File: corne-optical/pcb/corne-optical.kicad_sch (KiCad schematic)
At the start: 62 parts, among them J1 Conn_01x04, J2 Conn_01x03, J3 MJ-4PP-9, J4 Conn_01x01, J5 Conn_01x01, J6 Conn_01x02, J7 Conn_01x02, Q1 Q_NMOS_GSD, Q2 Q_NMOS_GSD, Q3 Q_NMOS_GSD, Q4 Q_NMOS_GSD, Q5 Q_NMOS_GSD, Q6 Q_NMOS_GSD, SW1 Keychron_LP_Optical, SW10 Keychron_LP_Optical, SW11 Keychron_LP_Optical, SW12 Keychron_LP_Optical, SW13 Keychron_LP_Optical, SW14 Keychron_LP_Optical, SW15 Keychron_LP_Optical, SW16 Keychron_LP_Optical, SW17 Keychron_LP_Optical, SW18 Keychron_LP_Optical, SW19 Keychron_LP_Optical, SW2 Keychron_LP_Optical, SW20 Keychron_LP_Optical, SW21 Keychron_LP_Optical, SW3 Keychron_LP_Optical, SW4 Keychron_LP_Optical, SW5 Keychron_LP_Optical, SW6 Keychron_LP_Optical, SW7 Keychron_LP_Optical, SW8 Keychron_LP_Optical, SW9 Keychron_LP_Optical, U1 ProMicro

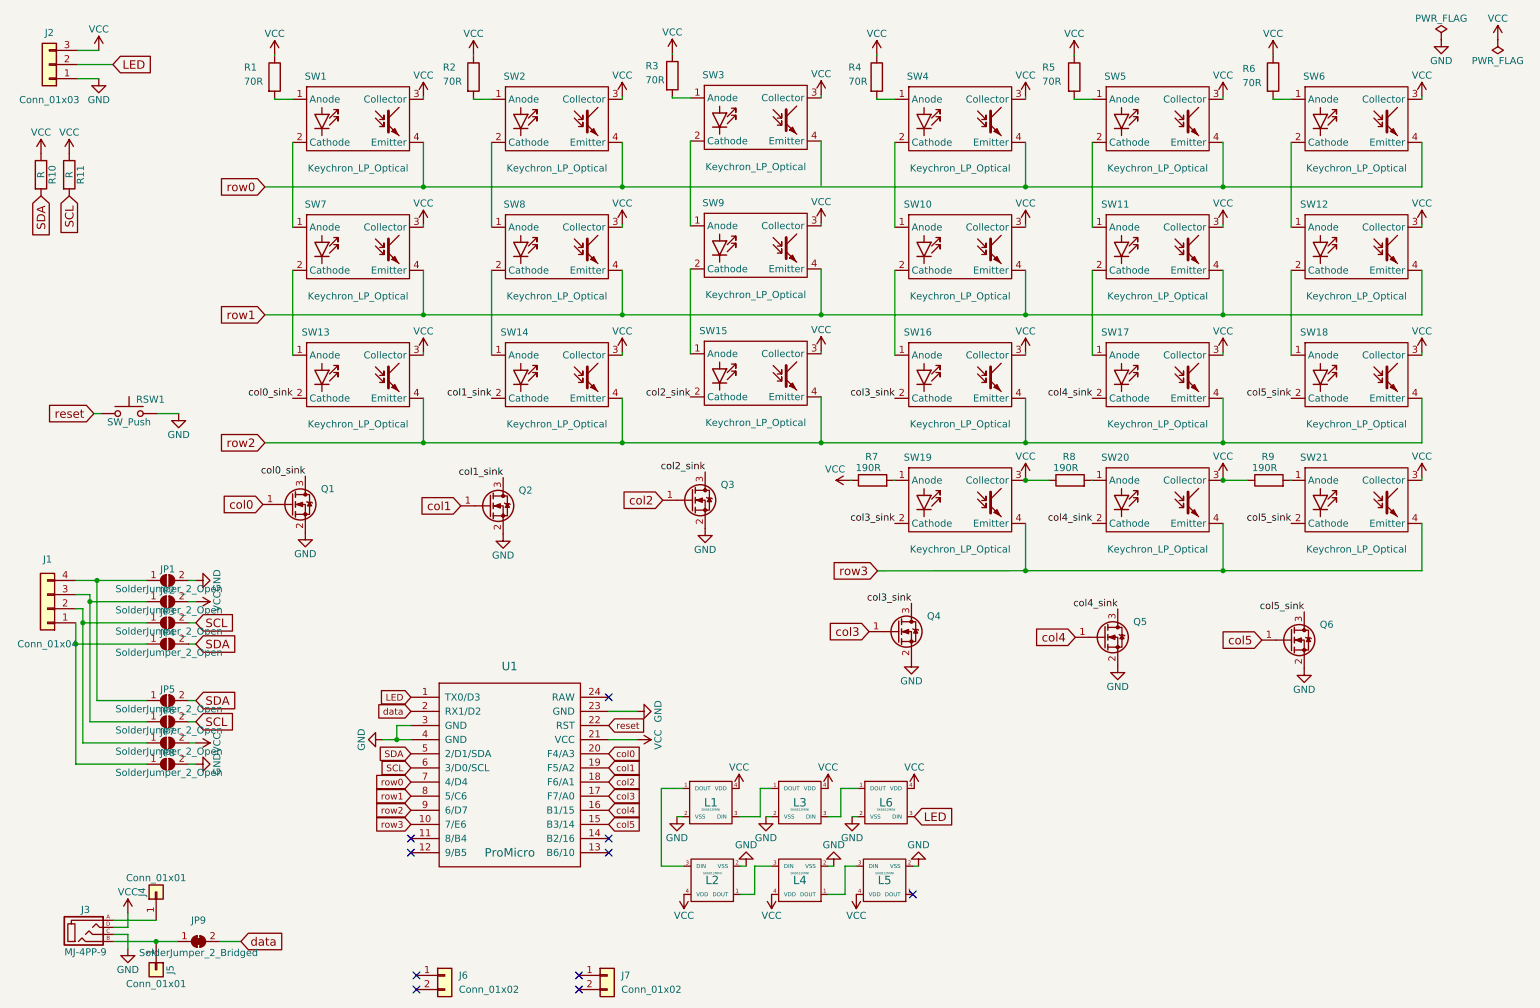
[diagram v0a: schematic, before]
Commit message: Fixed up designators on optical
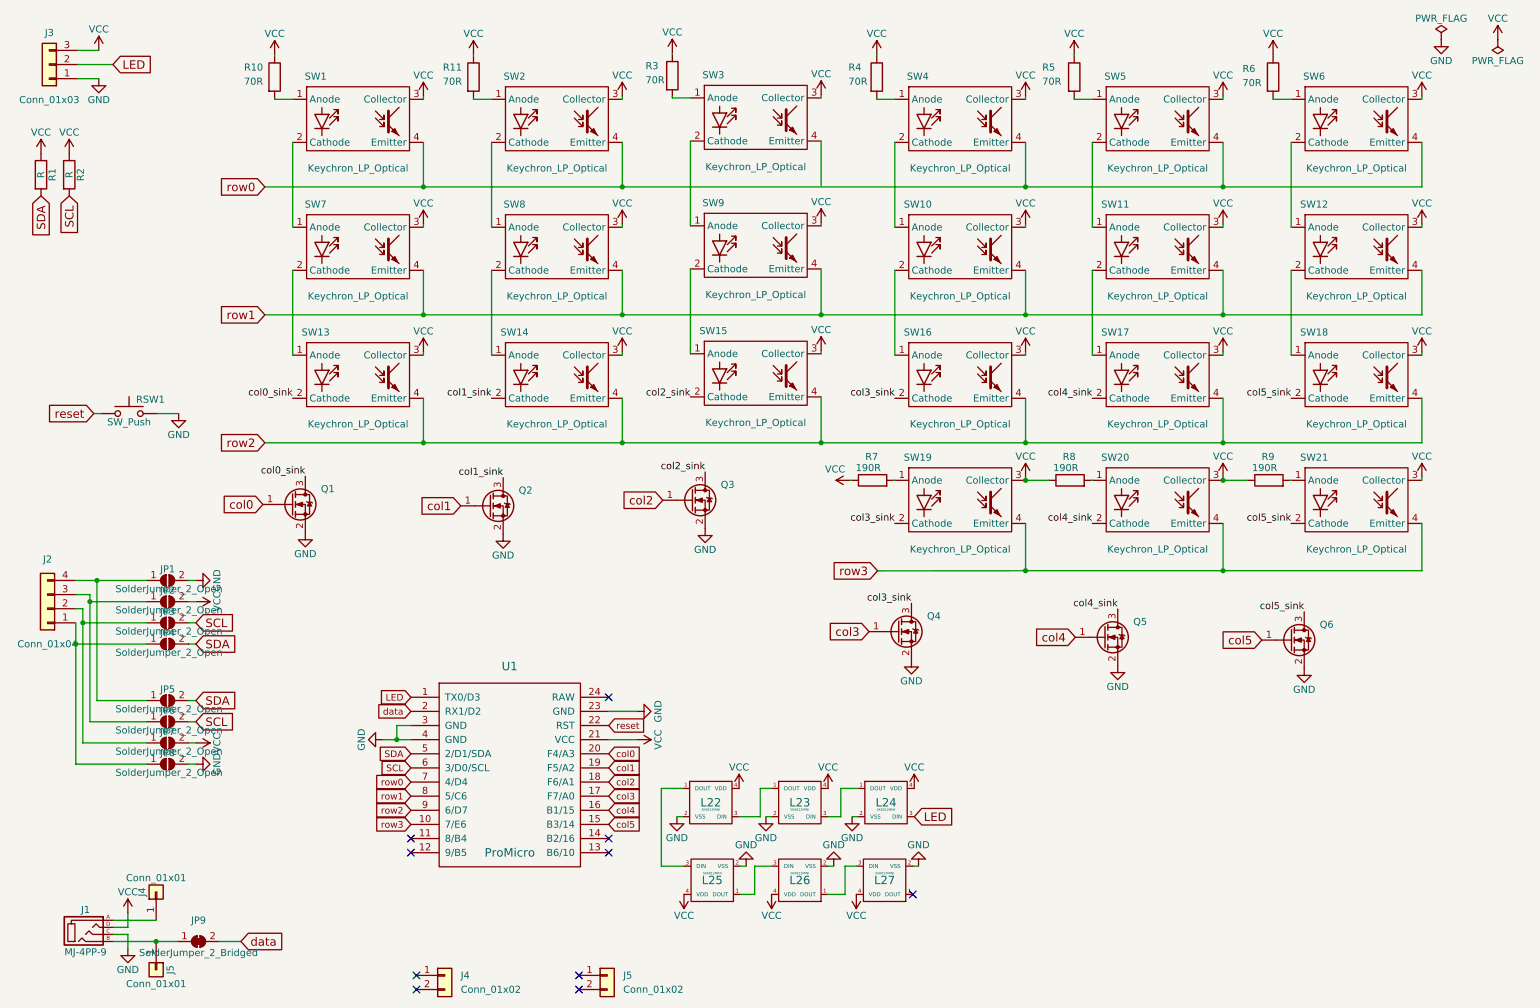
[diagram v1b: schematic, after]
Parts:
- renumbered J3 to J1, J1 to J2, J2 to J3, J6 to J4, J7 to J5, L1 to L22, L3 to L23, L6 to L24, L2 to L25, L4 to L26, L5 to L27, R10 to R1, R1 to R10, R2 to R11, R11 to R2

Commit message: Missed a few
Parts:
- renumbered JP9 to JP1, JP1 to JP9, J4 to P1, J5 to P2
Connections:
- net GND: now also JP2.2 (B); no longer JP8.2 (B)
- net SCL: now also JP4.2 (B), JP7.2 (B); no longer JP3.2 (B), JP6.2 (B)
- net SDA: now also JP6.2 (B); no longer JP4.2 (B)
- net VCC: now also JP3.2 (B), JP8.2 (B); no longer JP2.2 (B), JP7.2 (B)
- net at JP4.1 (A), JP8.1 (A): now also J2.2 (Pin_2); no longer J2.1 (Pin_1)
- net at JP3.1 (A), JP7.1 (A): now also J2.3 (Pin_3); no longer J2.2 (Pin_2)
- net at JP2.1 (A), JP6.1 (A): now also J2.4 (Pin_4); no longer J2.3 (Pin_3)
- net at JP5.1 (A), JP9.1 (A): now also J2.1 (Pin_1); no longer J2.4 (Pin_4)
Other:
- moved on the sheet: JP2, JP3, JP4, JP5, JP6, JP7, JP8, JP9

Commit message: Trying to workout phantom copper
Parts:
- removed L22, L23, L24, L25, L26, L27: SK6812MINI, kbd:SK6812MINI_underglow_rev, symbol kbd:SK6812MINI
- SW1, SW10, SW11, SW12, SW13, SW14, SW15, SW16, SW17, SW18, SW19, SW2, SW20, SW3, SW4, SW5, SW6, SW7, SW8, SW9: footprint kbd:Choc_Hotswap -> optical:Keychron_LP_Optical
- SW21: footprint kbd:Choc_Hotswap_1.5u -> optical:Keychron_LP_Optical_1.5u
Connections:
- no-connect marks 10 -> 9

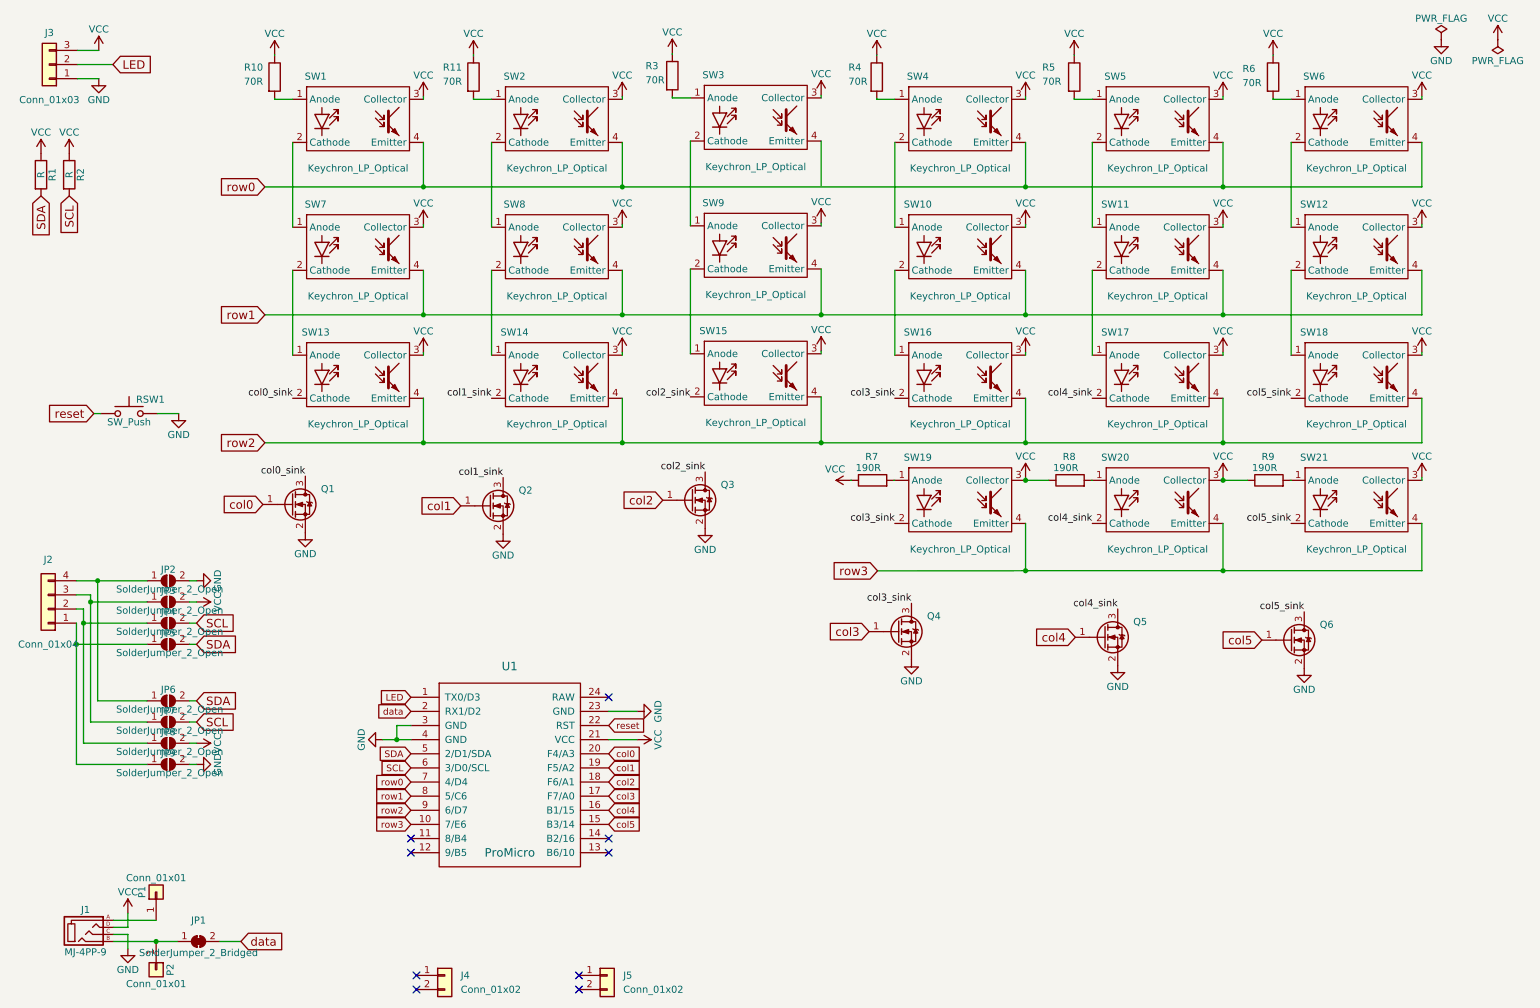
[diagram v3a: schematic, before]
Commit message: Fixed outline, just trying to solve switch footprint glitch
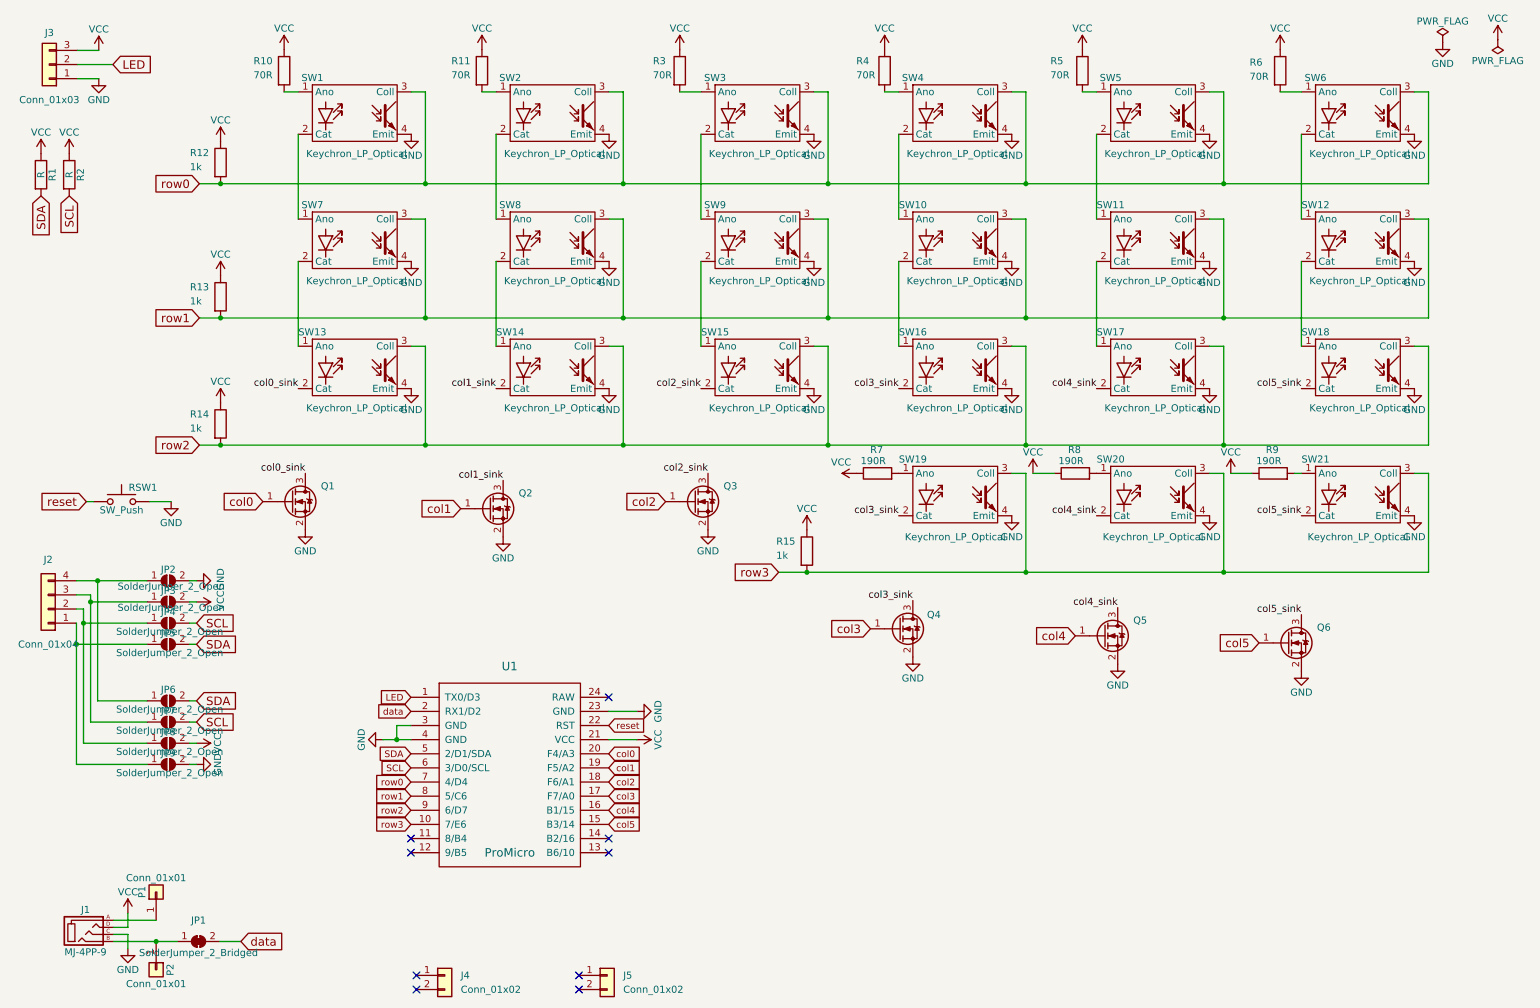
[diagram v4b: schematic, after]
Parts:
- added R12, R13, R14, R15: 1k, Resistor_SMD:R_0603_1608Metric, symbol Device:R
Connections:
- net GND: now also SW1.4 (Emit), SW10.4 (Emit), SW11.4 (Emit), SW12.4 (Emit), SW13.4 (Emit), SW14.4 (Emit), SW15.4 (Emit), SW16.4 (Emit), SW17.4 (Emit), SW18.4 (Emit), SW19.4 (Emit), SW2.4 (Emit), SW20.4 (Emit), SW21.4 (Emit), SW3.4 (Emit), SW4.4 (Emit), SW5.4 (Emit), SW6.4 (Emit), SW7.4 (Emit), SW8.4 (Emit), SW9.4 (Emit)
- net VCC: now also R12.1, R13.1, R14.1, R15.1; no longer SW1.3 (Collector), SW10.3 (Collector), SW11.3 (Collector), SW12.3 (Collector), SW13.3 (Collector), SW14.3 (Collector), SW15.3 (Collector), SW16.3 (Collector), SW17.3 (Collector), SW18.3 (Collector), SW19.3 (Collector), SW2.3 (Collector), SW20.3 (Collector), SW21.3 (Collector), SW3.3 (Collector), SW4.3 (Collector), SW5.3 (Collector), SW6.3 (Collector), SW7.3 (Collector), SW8.3 (Collector), SW9.3 (Collector)
- net col2_sink: now also SW15.2 (Cat)
- net row0: now also SW1.3 (Coll), SW2.3 (Coll), SW3.3 (Coll), SW4.3 (Coll), SW5.3 (Coll), SW6.3 (Coll), R12.2; no longer SW1.4 (Emitter), SW2.4 (Emitter), SW4.4 (Emitter), SW5.4 (Emitter), SW6.4 (Emitter)
- net row1: now also SW10.3 (Coll), SW11.3 (Coll), SW12.3 (Coll), SW7.3 (Coll), SW8.3 (Coll), SW9.3 (Coll), R13.2; no longer SW10.4 (Emitter), SW11.4 (Emitter), SW12.4 (Emitter), SW7.4 (Emitter), SW8.4 (Emitter), SW9.4 (Emitter)
- net row2: now also SW13.3 (Coll), SW14.3 (Coll), SW15.3 (Coll), SW16.3 (Coll), SW17.3 (Coll), SW18.3 (Coll), R14.2; no longer SW13.4 (Emitter), SW14.4 (Emitter), SW15.4 (Emitter), SW16.4 (Emitter), SW17.4 (Emitter), SW18.4 (Emitter)
- net row3: now also SW19.3 (Coll), SW20.3 (Coll), SW21.3 (Coll), R15.2; no longer SW19.4 (Emitter), SW20.4 (Emitter), SW21.4 (Emitter)
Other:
- moved on the sheet: Q1, Q2, Q3, Q4, Q6, R10, R11, R3, R4, R5, R6, R7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

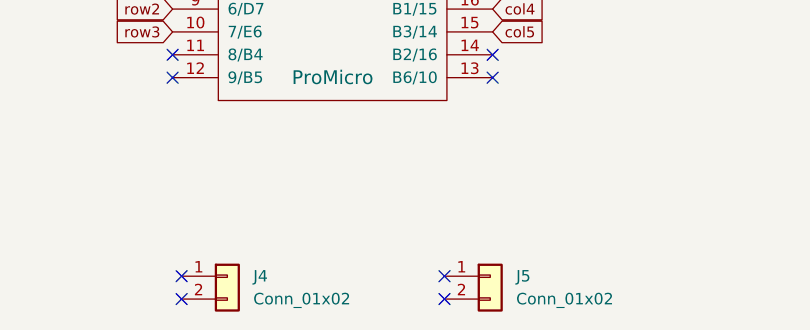
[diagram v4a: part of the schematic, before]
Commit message: Finished, but need to add mounting holes for plate
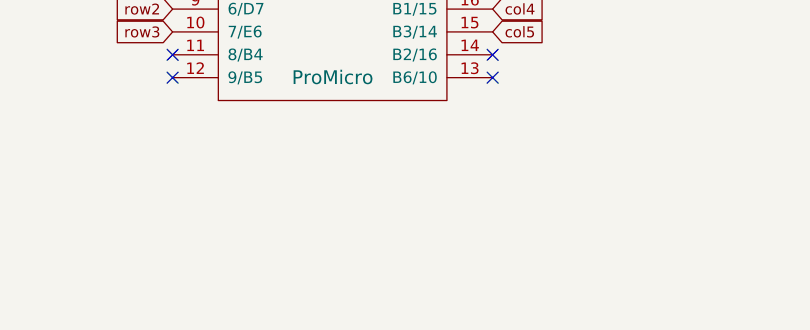
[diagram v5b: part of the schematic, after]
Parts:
- removed J4, J5: Conn_01x02, Connector_AMASS:AMASS_XT60-F_1x02_P7.20mm_Vertical, symbol Connector_Generic:Conn_01x02
- Q1, Q2, Q3, Q4, Q5, Q6: footprint Package_TO_SOT_SMD:SOT-23 -> optical:SOT-23
- R1, R2: footprint kbd:R -> optical:R_0603_1608Metric
- R10, R11, R12, R13, R14, R15, R3, R4, R5, R6, R7, R8, R9: footprint Resistor_SMD:R_0603_1608Metric -> optical:R_0603_1608Metric
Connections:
- no-connect marks 9 -> 5
